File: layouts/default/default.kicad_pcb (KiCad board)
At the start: 2 copper layers, 34 parts

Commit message: Upgrade to atopile 0.14 and use official mounting-holes package
- Bump requires-atopile to ^0.14.0, mounting-holes dep to 0.2.0
- Switch from local MountingHole_M3 workaround to official package
- Remove local parts/MountingHole_3_2_M3_Pad (now from package)
- Add S8050 NPN transistor part for upcoming auto-reset circuit
- Parts updated by atopile 0.14 build (traits, symbols, footprints)
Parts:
- added H1: , MountingHole_3_2_M3_Pad:MountingHole_3.2_M3_Pad, F.Cu at (0.00, 0.00)
- added H2: , MountingHole_3_2_M3_Pad:MountingHole_3.2_M3_Pad, F.Cu at (10.0, 0.00)
- added H3: , MountingHole_3_2_M3_Pad:MountingHole_3.2_M3_Pad, F.Cu at (20.0, 0.00)
- added H4: , MountingHole_3_2_M3_Pad:MountingHole_3.2_M3_Pad, F.Cu at (30.0, 0.00)
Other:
- board outline added: 50 x 50 mm

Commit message: board layout
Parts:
- added Q1: , Changjiang_Electronics_Tech_S8050_J3Y_RANGE_200_350:SOT-23-3_L3.0-W1.7-P0.95-LS2.9-BR, F.Cu at (0.00, 0.00)
- added Q2: , Changjiang_Electronics_Tech_S8050_J3Y_RANGE_200_350:SOT-23-3_L3.0-W1.7-P0.95-LS2.9-BR, F.Cu at (10.0, 0.00)
- added R15: 10000Ω, UNI_ROYAL_0603WAF1002T5E:R0603, F.Cu at (60.0, -10.0)
- added R16: 10000Ω, UNI_ROYAL_0603WAF1002T5E:R0603, F.Cu at (60.0, 0.00)
- C1, C2, C4: value 100nF ±10% 50V X7R -> 0F
- C3: value 1µF ±10% 50V X5R -> 0F
- C5: value 10µF ±10% 25V X5R -> 0F
- C6: value 22µF ±20% 25V X5R -> 0F
- C7, C8: value 22pF ±5% 50V C0G -> 0F
- R1, R2, R3, R4: value 5.1kΩ ±1% 100mW -> 5100Ω
- R10, R11, R12, R13, R14, R5, R7, R8, R9: value 10kΩ ±1% 100mW -> 10000Ω
- R6: value 1kΩ ±1% 100mW -> 1000Ω
- moved H1 40.0 mm to (40.0, 0.00)
- moved H2 40.0 mm to (50.0, 0.00)
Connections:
- net A6 renamed 18
- net A7 renamed 17
- net EN renamed en_cap-power-hv
- net GND renamed lv
- net IO0 renamed 12
- net IO1 renamed 13
- net IO14 renamed 19
- net IO15 renamed 20
- net IO18 renamed 24
- net IO19 renamed 25
- net IO2 renamed 4
- net IO20 renamed 26
- net IO21 renamed 27
- net IO22 renamed 28
- net IO23 renamed 29
- net IO3 renamed 5
- net IO4 renamed 6
- net IO5 renamed 10
- net IO6 renamed 15-1
- net IO7 renamed 16
- net IO8 renamed 22
- net IO9 renamed 2
- net R232 renamed 15
- net V3 renamed ch340g_v3_cap-power-hv
- net XI renamed xtal_c1-power-hv
- net XO renamed xtal_c2-power-hv
- net cc1_r_debug-A5 renamed A5
- net cc1_r_esp-A5 renamed A5-1
- net cc2_r_debug-B5 renamed B5
- net cc2_r_esp-B5 renamed B5-1
- net diode_debug-VBUS renamed VBUS
- net diode_esp-VBUS renamed VBUS-1
- net footprint-A8-0 renamed A8
- net footprint-A8-1 renamed usb_esp-A8
- net footprint-B8-0 renamed B8
- net footprint-B8-1 renamed usb_esp-B8
- net power_3v3-VCC renamed hv
- net power_5v-VCC renamed ldo_cin-power-hv
- U1 pad 13: nDTR -> C
- U1 pad 14: nRTS -> C-1
- U4 pad 21: esp32-net-0 -> (no net)
- U4 pad 32: esp32-net-1 -> (no net)
- U4 pad 33: esp32-net-2 -> (no net)
- U4 pad 34: esp32-net-3 -> (no net)
- U4 pad 35: esp32-net-4 -> (no net)
- U4 pad 4: esp32-net-5 -> (no net)
- U4 pad 7: esp32-net-6 -> (no net)
- USBC1 pad : footprint-net-0 -> (no net)
- USBC2 pad : footprint-net-1 -> (no net)

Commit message: Update PCB and passive footprints from ato build
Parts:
- C1, C2, C4: value 0F -> 100nF ±10% 50V X7R
- C3: value 0F -> 1µF ±10% 50V X5R
- C5: value 0F -> 10µF ±10% 25V X5R
- C6: value 0F -> 22µF ±20% 25V X5R
- C7, C8: value 0F -> 22pF ±5% 50V C0G
- R1, R2, R3, R4: value 5100Ω -> 5.1kΩ ±1% 100mW
- R10, R11, R12, R13, R14, R15, R16, R5, R7, R8, R9: value 10000Ω -> 10kΩ ±1% 100mW
- R6: value 1000Ω -> 1kΩ ±1% 100mW
- moved C8 340.5 mm to (111.0, 101.8), turned to 90 degrees
- moved USBC2 334.3 mm to (109.2, 116.0)
- moved C7 333.3 mm to (117.5, 101.8), turned to -90 degrees
- moved USBC1 331.6 mm to (127.9, 116.0)
- moved R6 280.7 mm to (103.8, 80.8)
- moved C5 280.4 mm to (102.5, 111.0), turned to 180 degrees
- moved C6 277.8 mm to (96.5, 100.5)
- moved U6 268.6 mm to (103.8, 77.8)
- moved U5 265.0 mm to (98.9, 105.9)
- moved C4 257.6 mm to (95.4, 109.2), turned to 180 degrees
- moved C3 239.3 mm to (136.5, 96.5), turned to -90 degrees
- moved R5 238.9 mm to (132.0, 89.1), turned to -90 degrees
- moved U4 234.2 mm to (104.0, 89.9), turned to 90 degrees
- moved U3 226.4 mm to (107.0, 109.5), turned to -90 degrees
- moved U2 225.7 mm to (119.1, 111.8)
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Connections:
- net 10 renamed IO5
- net 12 renamed IO0
- net 13 renamed IO1
- net 15 renamed R232
- net 15-1 renamed IO6
- net 16 renamed IO7
- net 17 renamed A7
- net 18 renamed A6
- net 19 renamed IO14
- net 2 renamed boot_pullup-E
- net 20 renamed IO15
- net 22 renamed IO8
- net 24 renamed IO18
- net 25 renamed IO19
- net 26 renamed IO20
- net 27 renamed IO21
- net 28 renamed IO22
- net 29 renamed IO23
- net 4 renamed IO2
- net 5 renamed IO3
- net 6 renamed IO4
- net A5 renamed cc1_r_debug-A5
- net A5-1 renamed cc1_r_esp-A5
- net A8 renamed footprint-A8-0
- net B renamed footprint-B-0
- net B-1 renamed footprint-B-1
- net B5 renamed cc2_r_debug-B5
- net B5-1 renamed cc2_r_esp-B5
- net B8 renamed footprint-B8-0
- net C renamed ch340g-C-0
- net C-1 renamed ch340g-C-1
- net VBUS renamed diode_debug-VBUS
- net VBUS-1 renamed diode_esp-VBUS
- net ch340g_v3_cap-power-hv renamed V3
- net en_cap-power-hv renamed btn_reset-E
- net hv renamed power_3v3-VCC
- net ldo_cin-power-hv renamed power_5v-VCC
- net lv renamed GND
- net usb_esp-A8 renamed footprint-A8-1
- net usb_esp-B8 renamed footprint-B8-1
- net xtal_c1-power-hv renamed XI
- net xtal_c2-power-hv renamed XO
- U4 pad 21: (no net) -> esp32-net-0
- U4 pad 32: (no net) -> esp32-net-1
- U4 pad 33: (no net) -> esp32-net-2
- U4 pad 34: (no net) -> esp32-net-3
- U4 pad 35: (no net) -> esp32-net-4
- U4 pad 4: (no net) -> esp32-net-5
- U4 pad 7: (no net) -> esp32-net-6
- USBC1 pad : (no net) -> footprint-net-0
- USBC2 pad : (no net) -> footprint-net-1
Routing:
- net power_3v3-VCC: track 0.00 -> 82.4 mm, vias 0 -> 2
- net power_5v-VCC: track 0.00 -> 67.3 mm, vias 0 -> 2
- net GND: track 0.00 -> 55.2 mm, vias 0 -> 42
- net IO2: track 0.00 -> 46.5 mm, vias 0 -> 2
- net btn_reset-E: track 0.00 -> 45.5 mm, vias 0 -> 2
- net IO4: track 0.00 -> 43.3 mm, vias 0 -> 3
- net boot_pullup-E: track 0.00 -> 37.9 mm, vias 0 -> 3
- net IO0: track 0.00 -> 36.7 mm, vias 0 -> 4
- net IO3: track 0.00 -> 36.2 mm, vias 0 -> 2
- net RXD: track 0.00 -> 33.2 mm, vias 0 -> 2
- net TXD: track 0.00 -> 31.5 mm, vias 0 -> 2
- net IO1: track 0.00 -> 27.6 mm, vias 0 -> 4
- net IO5: track 0.00 -> 27.0 mm
- net IO6: track 0.00 -> 26.9 mm, vias 0 -> 2
- net A7: track 0.00 -> 25.9 mm, vias 0 -> 2
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- added copper zone on B.Cu, net GND
- added copper zone on F.Cu, net GND

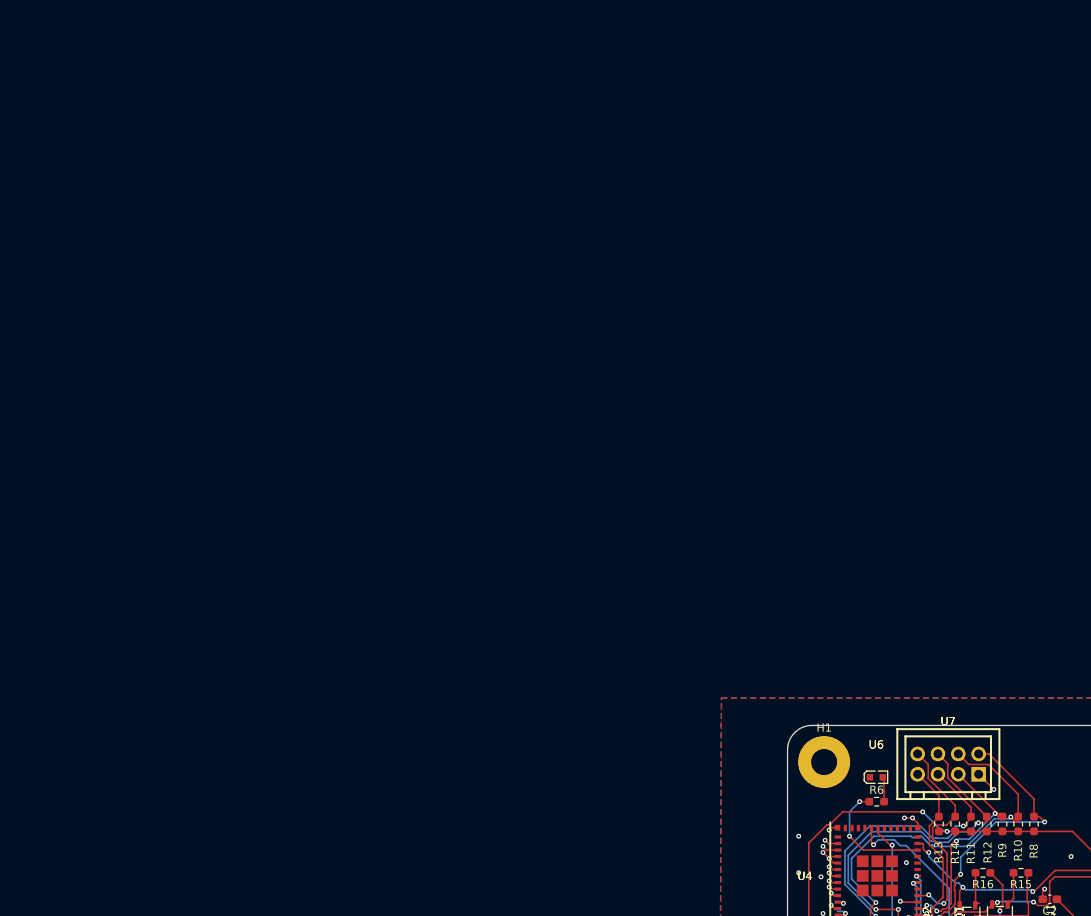
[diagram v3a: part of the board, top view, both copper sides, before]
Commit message: Replace 7 GPIO pullup resistors with two C29718 resistor arrays
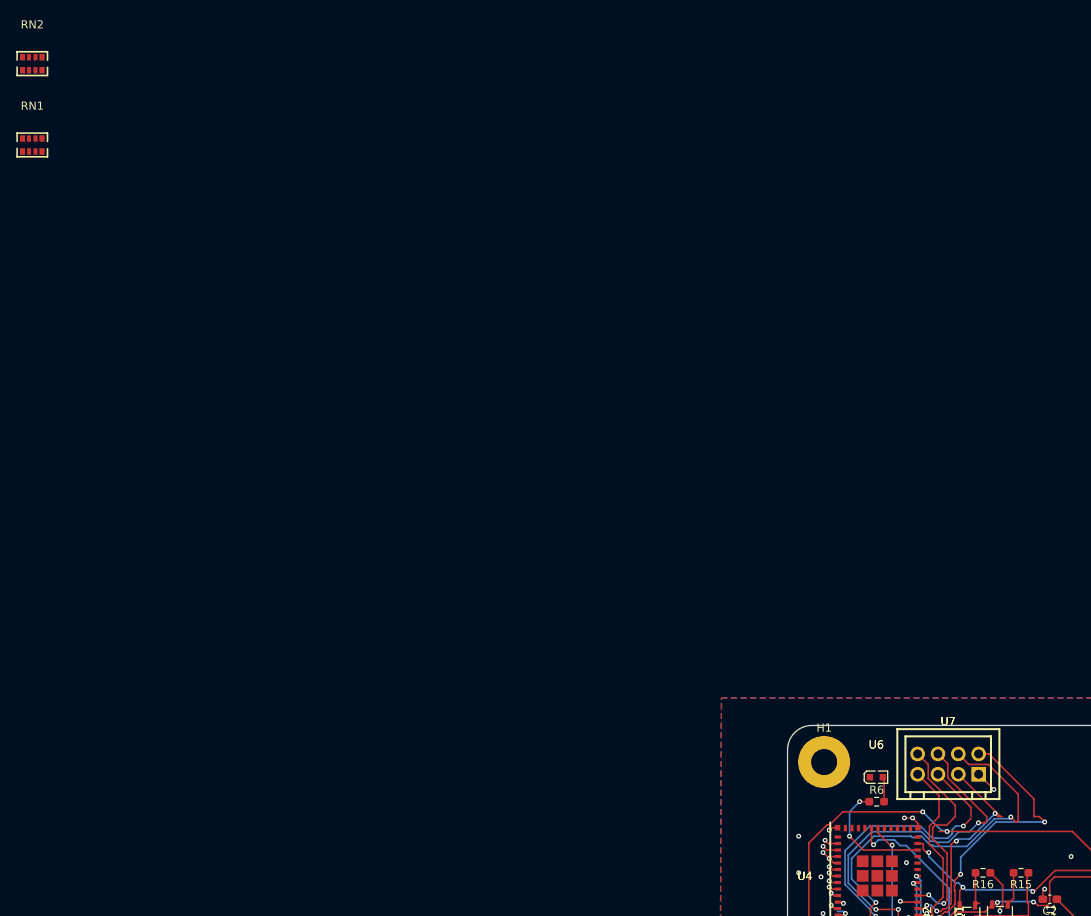
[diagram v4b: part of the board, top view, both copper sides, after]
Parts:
- removed R10, R11, R12, R13, R14, R8, R9: 10kΩ ±1% 100mW, UNI_ROYAL_0603WAF1002T5E:R0603
- added RN1: , UNI_ROYAL_4D03WGJ0103T5E:RES-ARRAY-SMD_0603-8P-L3.2-W1.6-BL, F.Cu at (0.00, 0.00)
- added RN2: , UNI_ROYAL_4D03WGJ0103T5E:RES-ARRAY-SMD_0603-8P-L3.2-W1.6-BL, F.Cu at (0.00, -10.0)
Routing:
- net (no net): track 0.00 -> 326.7 mm, vias 0 -> 19
- net power_3v3-VCC: track 82.4 -> 0.00 mm, vias 2 -> 0
- net IO2: track 46.5 -> 0.00 mm, vias 2 -> 0
- net IO4: track 43.3 -> 0.00 mm, vias 3 -> 0
- net IO0: track 36.7 -> 0.00 mm, vias 4 -> 0
- net IO3: track 36.2 -> 0.00 mm, vias 2 -> 0
- net IO1: track 27.6 -> 0.00 mm, vias 4 -> 0
- net IO5: track 27.0 -> 0.00 mm
- net IO6: track 26.9 -> 0.00 mm, vias 2 -> 0

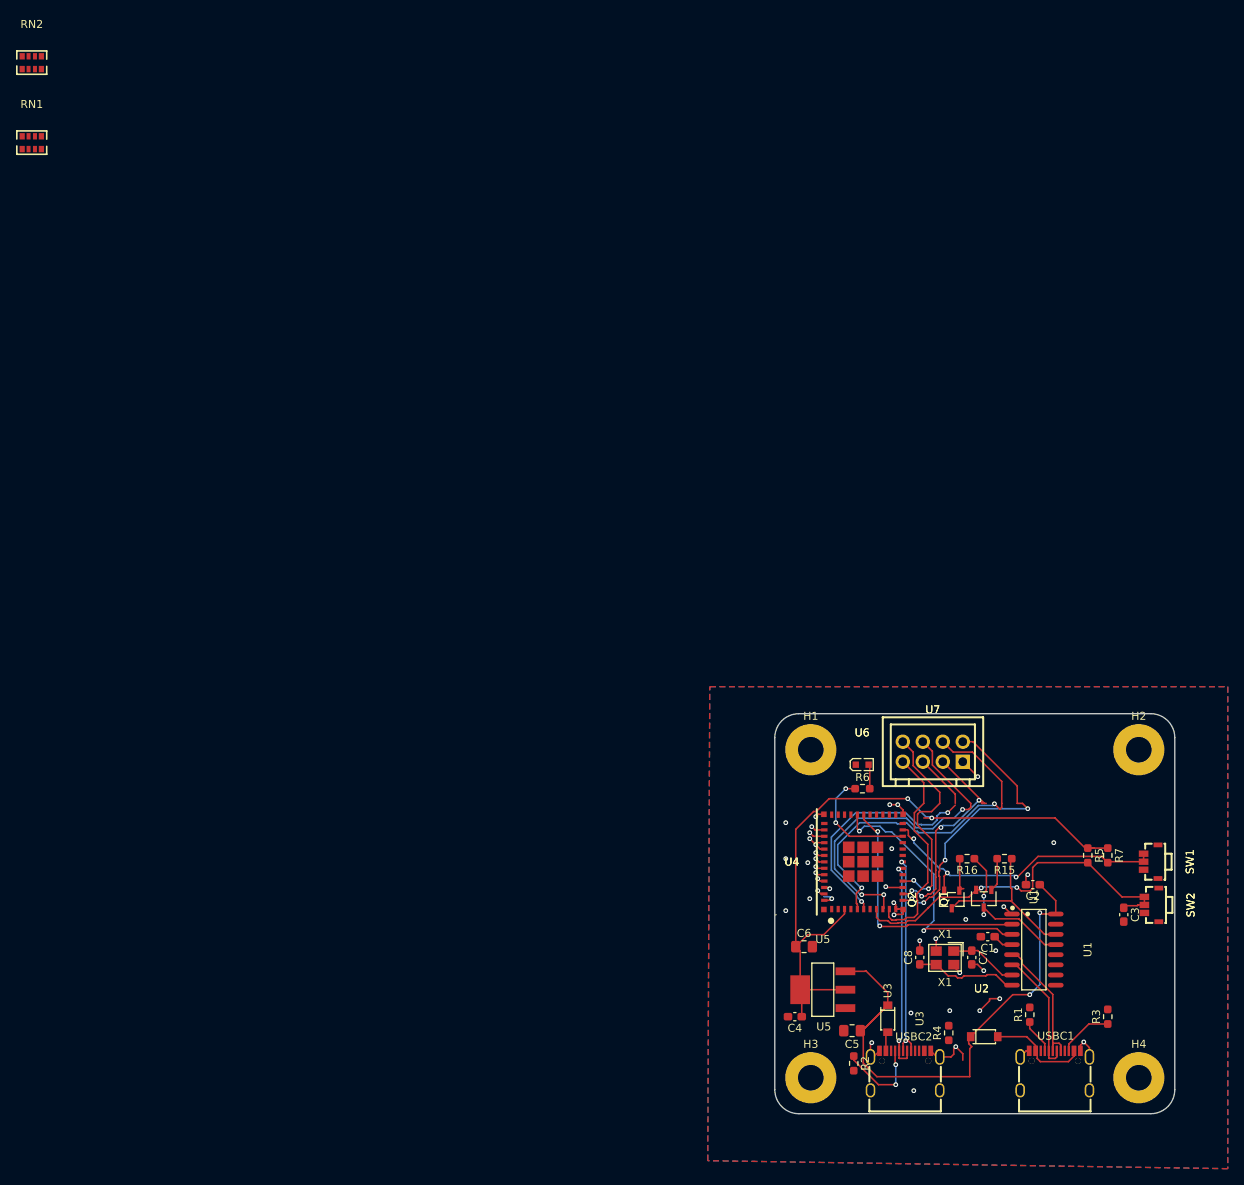
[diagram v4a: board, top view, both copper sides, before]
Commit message: Name USB signals with _P/_N suffixes for KiCad differential pair routing
Rename USB-C connector D+/D- signals (DP1/DN1 → D_P/D_N) and CH340G
signals (UDpos/UDneg → UD_P/UD_N) so KiCad auto-detects both USB
differential pairs (esp32-D_P/N and ch340g-D_P/N).

Also reorder RN1/RN2 pullup array GPIO assignments so pin order
descends left-to-right matching the header physical layout.
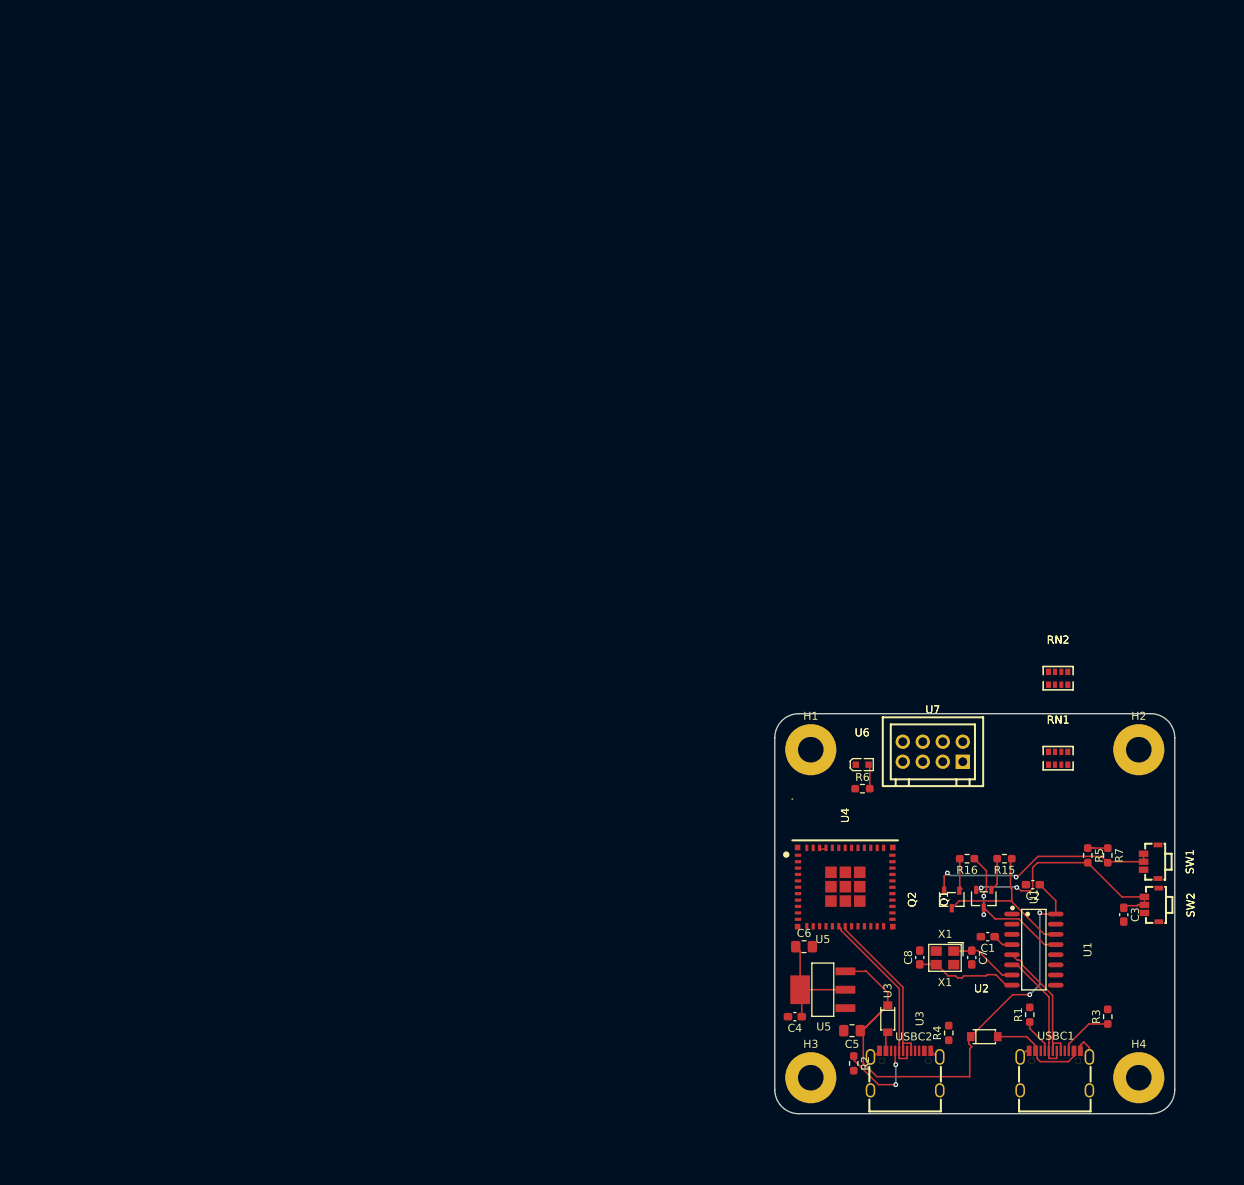
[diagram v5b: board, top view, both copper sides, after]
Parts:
- moved RN1 149.6 mm to (128.3, 77.0)
- moved RN2 149.6 mm to (128.3, 67.0)
- moved U4 3.89 mm to (101.7, 93.0), turned to 0 degrees
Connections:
- net A6 renamed esp32-D_P
- net A7 renamed esp32-D_N
- net UDneg renamed ch340g-D_N
- net UDpos renamed ch340g-D_P
- RN1 pad 6: IO2 -> IO4
- RN1 pad 7: IO1 -> IO5
- RN1 pad 8: IO0 -> IO6
- RN2 pad 6: IO6 -> IO0
- RN2 pad 7: IO5 -> IO1
- RN2 pad 8: IO4 -> IO2
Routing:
- net (no net): track 326.7 -> 0.00 mm, vias 19 -> 0
- net GND: track 55.2 -> 7.55 mm, vias 42 -> 0
- net RXD: track 33.2 -> 0.00 mm, vias 2 -> 0
- net TXD: track 31.5 -> 0.00 mm, vias 2 -> 0
- net power_3v3-VCC: track 0.00 -> 18.0 mm
- net btn_reset-E: track 45.5 -> 29.6 mm
- net IO8: track 15.0 -> 0.00 mm, vias 2 -> 0
- net boot_pullup-E: track 37.9 -> 29.5 mm, vias 3 -> 2
- net esp32-D_P: track 25.8 -> 21.4 mm, vias 2 -> 0
- net esp32-D_N: track 25.9 -> 21.6 mm, vias 2 -> 0
- net ch340g-D_P: track 16.5 -> 17.1 mm
- removed copper zone on B.Cu, net GND
- removed copper zone on F.Cu, net GND

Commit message: Layout quasi ok.
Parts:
- moved RN1 18.4 mm to (110.8, 82.7)
- moved RN2 11.0 mm to (122.7, 76.5), turned to 90 degrees
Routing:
- net power_3v3-VCC: track 18.0 -> 86.8 mm, vias 0 -> 2
- net IO1: track 0.00 -> 48.8 mm, vias 0 -> 2
- net IO0: track 0.00 -> 44.8 mm, vias 0 -> 1
- net IO2: track 0.00 -> 44.6 mm, vias 0 -> 1
- net IO4: track 0.00 -> 36.0 mm
- net IO6: track 0.00 -> 35.6 mm, vias 0 -> 1
- net IO5: track 0.00 -> 35.0 mm, vias 0 -> 1
- net IO3: track 0.00 -> 30.2 mm, vias 0 -> 2
- net btn_reset-E: track 29.6 -> 51.4 mm, vias 2 -> 3
- net GND: track 7.55 -> 28.3 mm, vias 0 -> 26
- net IO8: track 0.00 -> 18.3 mm, vias 0 -> 2
- net RXD: track 0.00 -> 17.7 mm, vias 0 -> 2
- net TXD: track 0.00 -> 17.2 mm, vias 0 -> 2
- net boot_pullup-E: track 29.5 -> 40.5 mm
- net diode_esp-VBUS: track 2.10 -> 9.67 mm
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- added copper zone on B.Cu, net GND
- added copper zone on F.Cu, net GND

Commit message: update
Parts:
- U7: footprint chxunda_XD_XHD_2_4A:CONN-TH_XD-XHD-2-4A -> BOOMELE_2_54_1_10P:HDR-TH_10P-P2.54-V-M-1
- moved C3 5.70 mm to (132.0, 93.0)
- moved R2 3.10 mm to (102.5, 112.0), turned to 180 degrees
- moved C2 1.36 mm to (126.5, 92.8)
- moved C5 1.00 mm to (102.5, 110.0)
- moved C6 0.50 mm to (96.5, 101.0)
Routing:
- net GND: track 28.3 -> 56.4 mm, vias 26 -> 47
- net footprint-net-0: track 0.00 -> 6.81 mm
- net footprint-net-1: track 0.00 -> 6.69 mm
- net IO1: track 48.8 -> 55.4 mm
- net power_5v-VCC: track 67.1 -> 60.6 mm, vias 2 -> 8
- net cc1_r_esp-A5: track 11.3 -> 5.68 mm
- net IO0: track 44.8 -> 50.3 mm
- net power_3v3-VCC: track 86.8 -> 81.7 mm, vias 2 -> 4
- net ch340g-D_N: track 15.3 -> 17.6 mm
- net IO6: track 35.6 -> 38.0 mm
- net btn_reset-E: track 51.4 -> 53.1 mm
- net IO5: track 35.0 -> 33.5 mm
- net diode_debug-VBUS: track 12.3 -> 13.5 mm, vias 0 -> 2
- net ch340g-D_P: track 17.1 -> 18.0 mm
- net IO4: track 36.0 -> 36.8 mm
- added copper zone on F.Cu, net A
- added copper zone on B.Cu, net IO0
- added copper zone on F.Cu, net IO0
- added copper zone on B.Cu, net IO1
- added copper zone on F.Cu, net IO1
- added copper zone on B.Cu, net IO2
- added copper zone on F.Cu, net IO2
- added copper zone on B.Cu, net IO3
- added copper zone on F.Cu, net IO3
- added copper zone on F.Cu, net IO4
- added copper zone on B.Cu, net IO5
- added copper zone on F.Cu, net IO5
- added copper zone on B.Cu, net IO6
- added copper zone on F.Cu, net IO6
- added copper zone on B.Cu, net IO8
- added copper zone on F.Cu, net IO8
- added copper zone on B.Cu, net RXD
- added copper zone on F.Cu, net RXD
- added copper zone on B.Cu, net TXD
- added copper zone on F.Cu, net TXD
- added copper zone on F.Cu, net V3
- added copper zone on F.Cu, net XI
- added copper zone on F.Cu, net XO
- added copper zone on B.Cu, net boot_pullup-E
- added copper zone on F.Cu, net boot_pullup-E
- added copper zone on B.Cu, net btn_reset-E
- added copper zone on F.Cu, net btn_reset-E
- added copper zone on F.Cu, net cc1_r_debug-A5
- added copper zone on B.Cu, net cc1_r_esp-A5
- added copper zone on F.Cu, net cc1_r_esp-A5
- added copper zone on F.Cu, net cc2_r_debug-B5
- added copper zone on F.Cu, net cc2_r_esp-B5
- added copper zone on B.Cu, net ch340g-C-0
- added copper zone on F.Cu, net ch340g-C-0
- added copper zone on F.Cu, net ch340g-C-1
- added copper zone on F.Cu, net ch340g-D_N
- added copper zone on F.Cu, net ch340g-D_P
- added copper zone on F.Cu, net diode_debug-VBUS
- added copper zone on F.Cu, net diode_esp-VBUS
- added copper zone on F.Cu, net esp32-D_N
- added copper zone on F.Cu, net esp32-D_P
- added copper zone on F.Cu, net footprint-B-0
- added copper zone on F.Cu, net footprint-B-1
- added copper zone on F.Cu, net footprint-net-0
- added copper zone on F.Cu, net footprint-net-1
- added copper zone on B.Cu, net power_3v3-VCC
- added copper zone on F.Cu, net power_3v3-VCC
- added copper zone on B.Cu, net power_5v-VCC
- added copper zone on F.Cu, net power_5v-VCC
